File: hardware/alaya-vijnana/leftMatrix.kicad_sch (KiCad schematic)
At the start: 42 parts, among them SW10 MX HotSwap, SW11 MX HotSwap, SW12 MX HotSwap, SW13 MX HotSwap, SW14 MX HotSwap, SW15 MX HotSwap, SW16 MX HotSwap, SW17 MX HotSwap, SW18 MX HotSwap, SW19 MX HotSwap, SW2 MX HotSwap, SW20 MX HotSwap, SW21 MX HotSwap, SW22 MX HotSwap, SW3 MX HotSwap, SW4 MX HotSwap, SW5 MX HotSwap, SW6 MX HotSwap, SW7 MX HotSwap, SW8 MX HotSwap, SW9 MX HotSwap

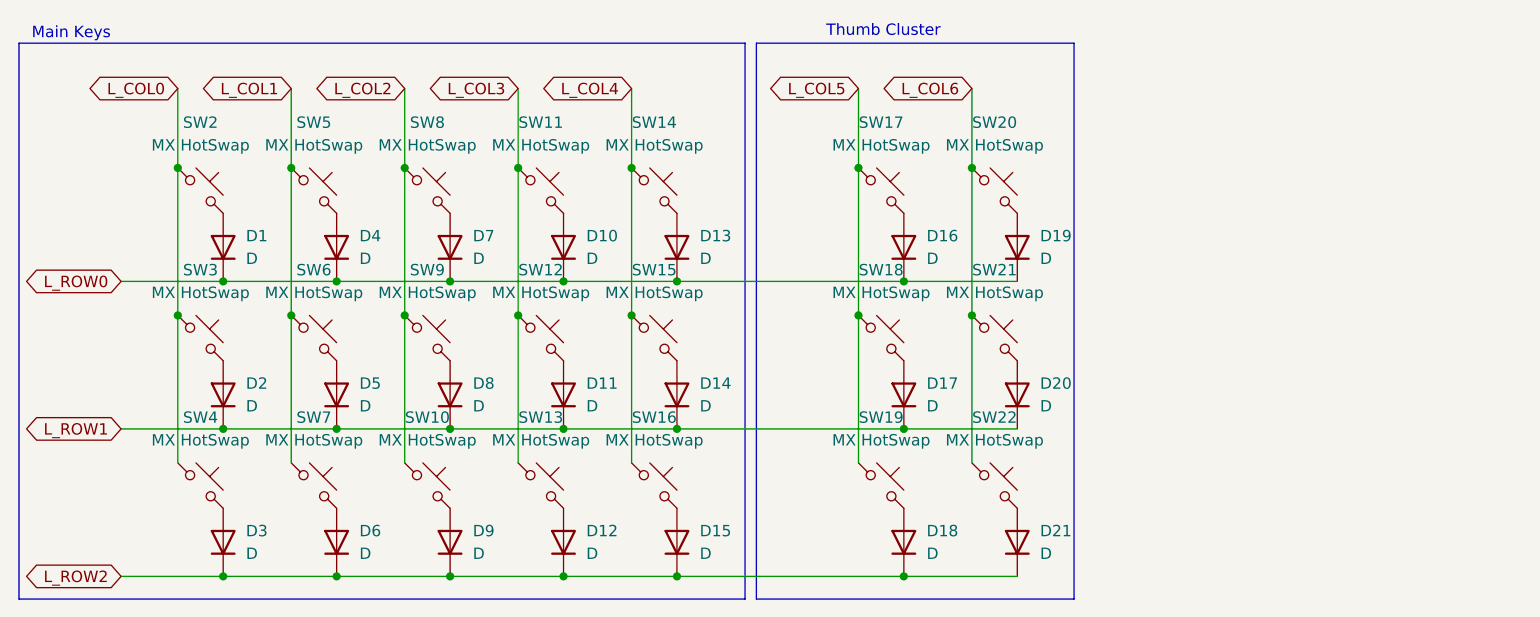
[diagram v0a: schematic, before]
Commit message: finished key wiring w/ connectors
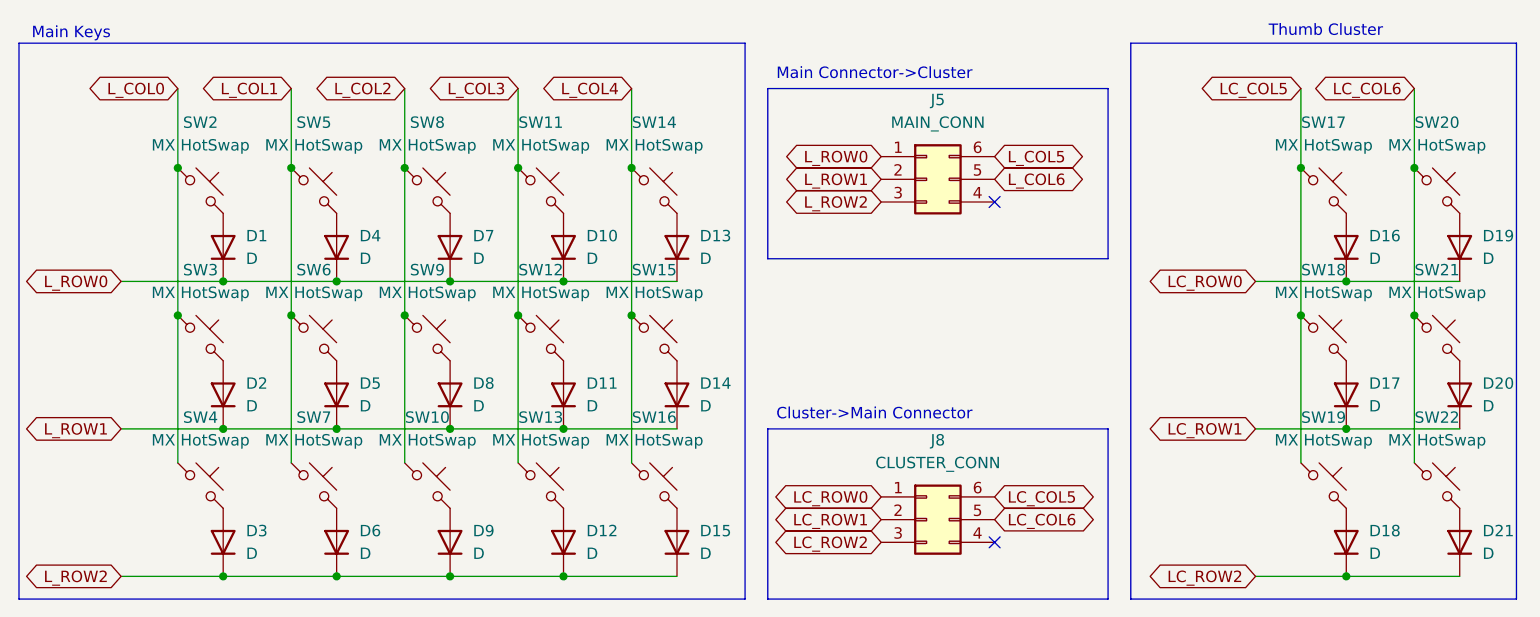
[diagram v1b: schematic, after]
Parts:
- added J5: MAIN_CONN, Connector_IDC:IDC-Header_2x03_P2.54mm_Horizontal, symbol Connector_Generic:Conn_02x03_Counter_Clockwise
- added J8: CLUSTER_CONN, Connector_IDC:IDC-Header_2x03_P2.54mm_Horizontal, symbol Connector_Generic:Conn_02x03_Counter_Clockwise
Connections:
- net L_COL5: now also J5.6 (Pin_6); no longer SW17.1, SW18.1, SW19.1
- net L_COL6: now also J5.5 (Pin_5); no longer SW20.1, SW21.1, SW22.1
- net L_ROW0: now also J5.1 (Pin_1); no longer D16.1 (K), D19.1 (K)
- net L_ROW1: now also J5.2 (Pin_2); no longer D17.1 (K), D20.1 (K)
- net L_ROW2: now also J5.3 (Pin_3); no longer D18.1 (K), D21.1 (K)
- new net LC_COL5: J8.6 (Pin_6), SW17.1, SW18.1, SW19.1
- new net LC_COL6: J8.5 (Pin_5), SW20.1, SW21.1, SW22.1
- new net LC_ROW0: D16.1 (K), D19.1 (K), J8.1 (Pin_1)
- new net LC_ROW1: D17.1 (K), D20.1 (K), J8.2 (Pin_2)
- new net LC_ROW2: D18.1 (K), D21.1 (K), J8.3 (Pin_3)
- no-connect marks 0 -> 2
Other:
- note added: "Cluster->Main Connector"
- note added: "Main Connector->Cluster"
- moved on the sheet: D16, D17, D18, D19, D20, D21, SW17, SW18, SW19, SW20, SW21, SW22
